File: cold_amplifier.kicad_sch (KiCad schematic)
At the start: 46 parts, among them Q1 BFP640, U1 THS4531AID

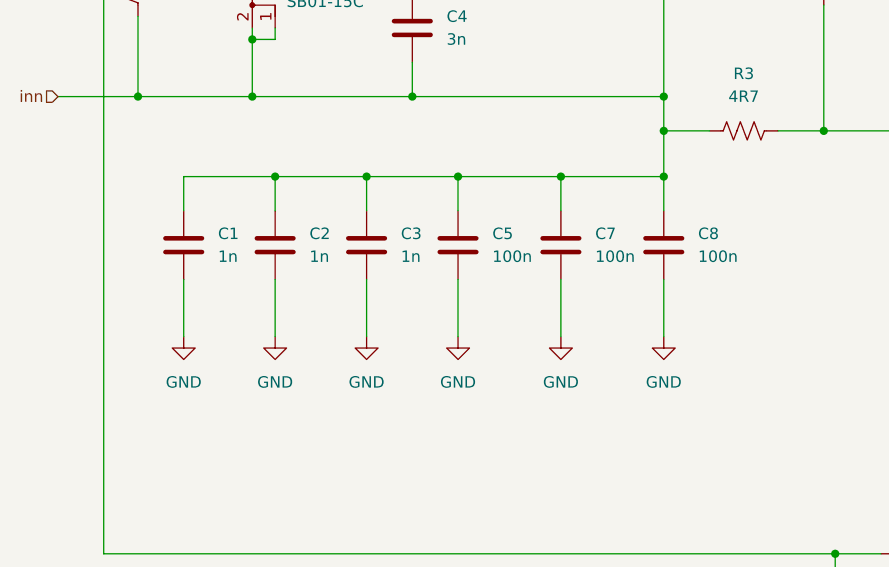
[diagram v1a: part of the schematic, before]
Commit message: Removed one pair of 1nF and 100nF capacitors connected to pin 2 of the BFP640 to allow the 100nF to be closer to the pin
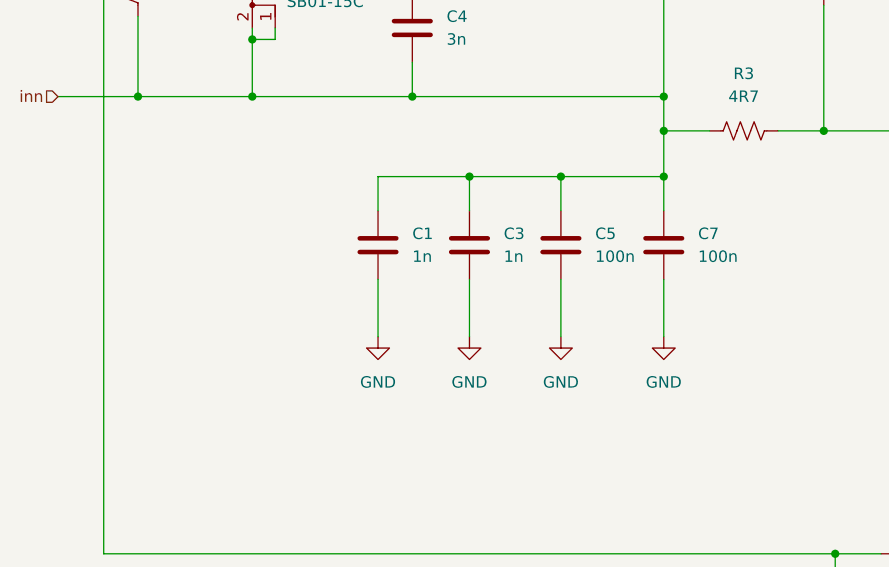
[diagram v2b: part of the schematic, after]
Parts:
- removed C2: 1n, Capacitor_SMD:C_0603_1608Metric, symbol Device:C
- removed C8: 100n, Capacitor_SMD:C_1206_3216Metric, symbol Device:C
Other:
- moved on the sheet: C1, C3, C5, C7

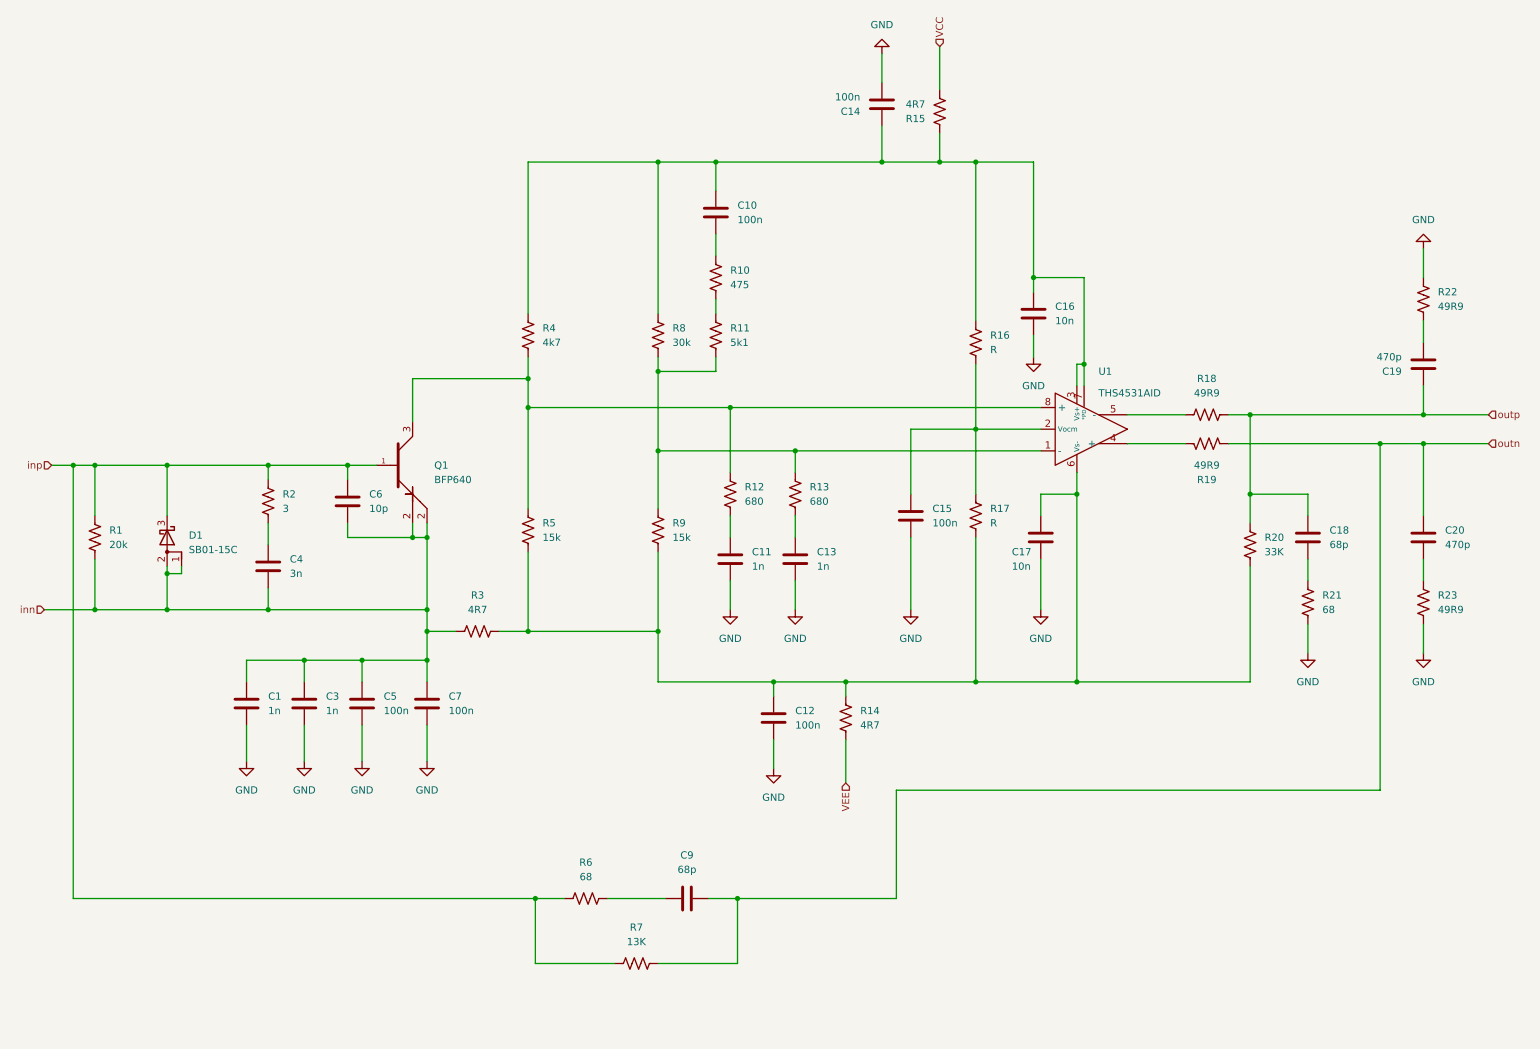
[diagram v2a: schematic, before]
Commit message: Moved connectors SiPM flex connectorsto both sides; rectangular vias stitching pattern
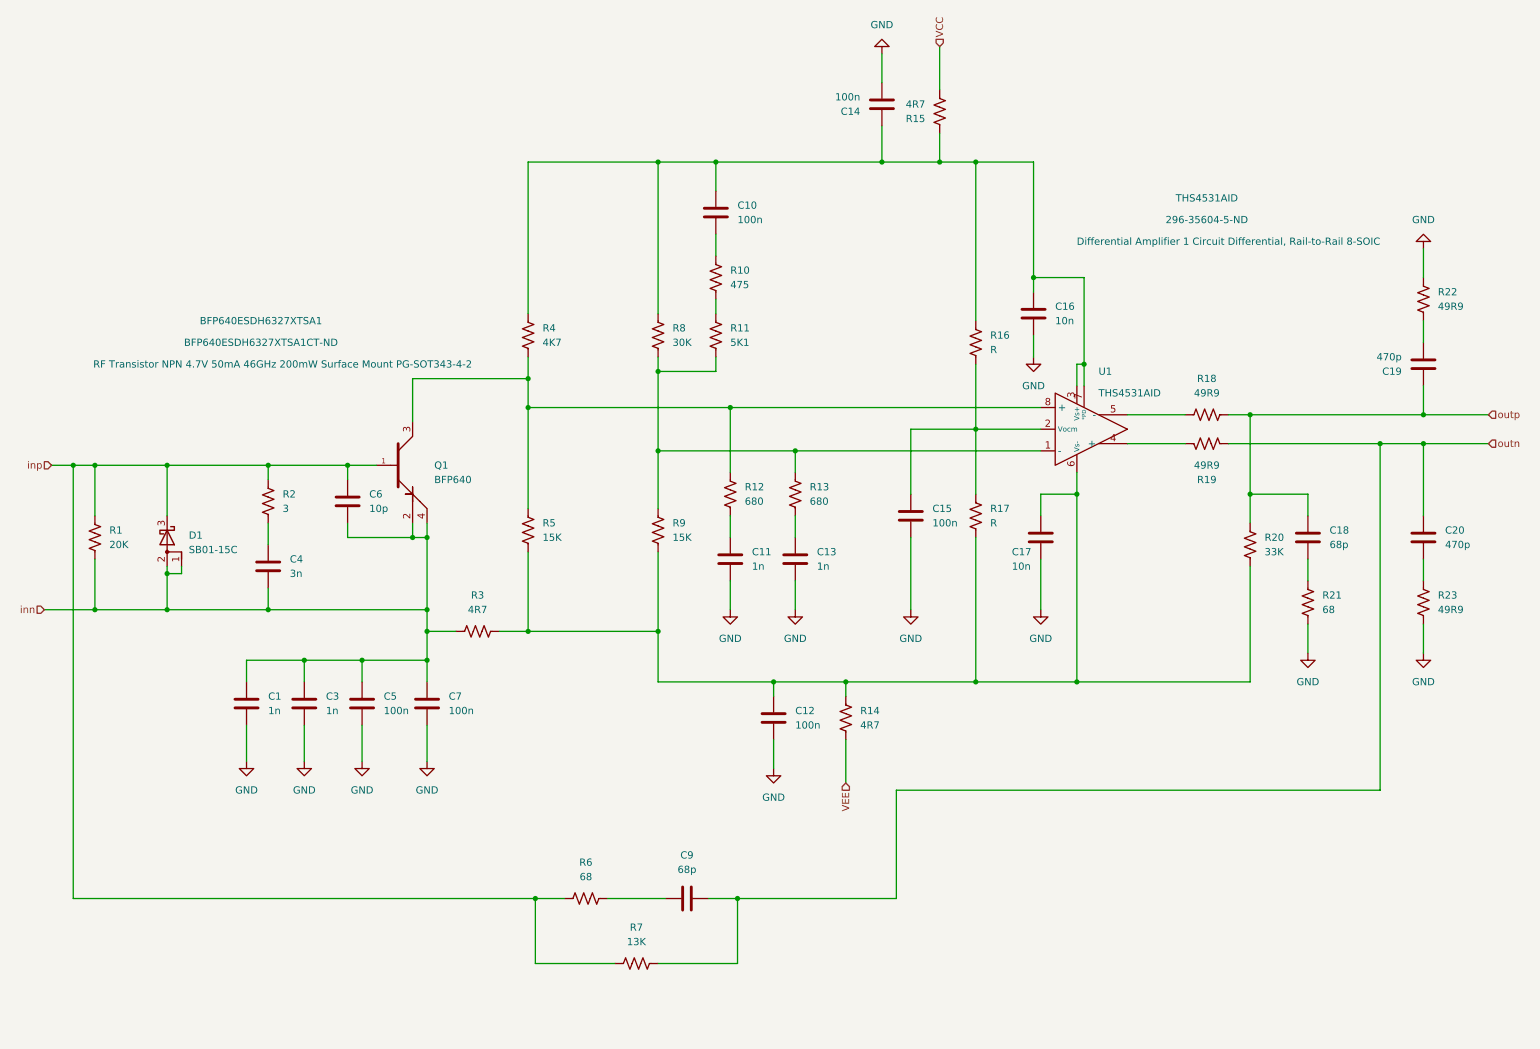
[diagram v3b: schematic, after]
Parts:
- C10, C12, C14, C15, C5, C7: Digikey Part Number (none) -> 490-GRM3195C2A104JA01DCT-ND; Manufacturer (none) -> Murata Electronics; Part Number (none) -> GRM3195C2A104JA01D
- D1: Digikey Part Number (none) -> SB01-15C-TB-EOSCT-ND; Part Number  (none) -> SB01-15C-TB-E
- Q1: Description  (none) -> RF Transistor NPN 4.7V 50mA 46GHz 200mW Surface Mount PG-SO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; Digikey Part Number (none) -> BFP640ESDH6327XTSA1CT-ND; Part Number (none) -> BFP640ESDH6327XTSA1
- R1: value 20k -> 20K; Digikey Part Number (none) -> P20KDACT-ND; Manufacturer (none) -> Panasonic Electronic Components; Part Number (none) -> ERA-6AEB203V
- R10: Digikey Part Number (none) -> P475DACT-ND; Manufacturer (none) -> Panasonic Electronic Components; Part Number (none) -> ERA-6AEB4750V
- R11: value 5k1 -> 5K1; Digikey Part Number (none) -> P5.1KDACT-ND; Manufacturer (none) -> Panasonic Electronic Components; Part Number (none) -> ERA-6AEB512V
- R12, R13: Digikey Part Number (none) -> P680DACT-ND; Manufacturer (none) -> Panasonic Electronic Components; Part Number (none) -> ERA-6AEB681V
- R14, R15, R3: Digikey Part Number (none) -> RNCP0805FTD4R70CT-ND; Manufacturer (none) -> Stackpole Electronics Inc; Part Number (none) -> RNCP0805FTD4R70
- R18, R19, R22, R23: Digikey Part Number (none) -> P49.9DACT-ND; Manufacturer (none) -> Panasonic Electronic Components; Part Number (none) -> ERA-6AEB49R9V
- R2: Digikey Part Number (none) -> YAG5007CT-ND; Manufacturer (none) -> YAGEO; Part Number (none) -> RT0805DRD073RL
- R20: Digikey Part Number (none) -> P33KDACT-ND; Manufacturer (none) -> Panasonic Electronic Components; Part Number (none) -> ERA-6AEB333V
- R21, R6: Digikey Part Number (none) -> P68DACT-ND; Manufacturer (none) -> Panasonic Electronic Components; Part Number (none) -> ERA-6AEB680V
- R4: value 4k7 -> 4K7; Digikey Part Number (none) -> P4.7KDACT-ND; Manufacturer (none) -> Panasonic Electronic Components; Part Number (none) -> ERA-6AEB472V
- R5: value 15k -> 15K; Digikey Part Number (none) -> YAG1787CT-ND; Manufacturer (none) -> YAGEO; Part Number  (none) -> RT0805BRD0715KL
- R7: Digikey Part Number (none) -> P13KDACT-ND; Manufacturer (none) -> Panasonic Electronic Components; Part Number (none) -> ERA-6AEB133V
- R8: value 30k -> 30K; Digikey Part Number (none) -> P30KDACT-ND; Manufacturer (none) -> Panasonic Electronic Components; Part Number (none) -> ERA-6AEB303V
- R9: value 15k -> 15K; Digikey Part Number (none) -> YAG1787CT-ND; Manufacturer (none) -> YAGEO; Part Number (none) -> RT0805BRD0715KL
- U1: Digikey Part Number (none) -> 296-35604-5-ND; Part Number (none) -> THS4531AID
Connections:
- net inn: now also Q1.4

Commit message: completed BOM list; replaced 47u with 33u capacitor
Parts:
- C1, C11, C13, C3: Digikey Part Number (none) -> 490-1451-1-ND; Manufacturer (none) -> Murata Electronics; Part Number (none) -> GRM1885C1H102JA01D
- C10, C12, C14, C15, C5, C7: Digikey Part Number 490-GRM3195C2A104JA01DCT-ND -> 490-6505-1-ND; Part Number GRM3195C2A104JA01D -> GRM31C5C1H104JA01L
- C16, C17: Digikey Part Number (none) -> 490-9666-1-ND; Manufacturer (none) -> Murata Electronics; Part Number (none) -> GRM1885C1H103JA01D
- C18, C9: Digikey Part Number (none) -> 1276-1135-1-ND; Manufacturer (none) -> Samsung Electro-Mechanics; Part Number (none) -> CL10C680JB8NNNC
- C19, C20: Digikey Part Number (none) -> 1276-1168-1-ND; Manufacturer (none) -> Samsung Electro-Mechanics; Part Number (none) -> CL10C471JB8NNNC
- C4: Digikey Part Number (none) -> 490-GCM1885C1H302FA16JCT-ND; Manufacturer (none) -> Murata Electronics; Part Number (none) -> GCM1885C1H302FA16J
- C6: Digikey Part Number (none) -> 490-4766-1-ND; Manufacturer (none) -> Murata Electronics; Part Number (none) -> GCM1885C1H100JA16D
- D1: value SB01-15C -> BAR46FILM; Digikey Part Number SB01-15C-TB-EOSCT-ND -> 497-12128-1-ND; Manufacturer (none) -> STMicroelectronics; Part Number (none) -> BAR46FILM; Part Number  SB01-15C-TB-E -> (none)
- Q1: Description  RF Transistor NPN 4.7V 50mA 46GHz 200mW Surface Mount PG-SO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 -> (none); Manufacturer (none) -> Infineon Technologies
- R5: Part Number (none) -> RT0805BRD0715KL; Part Number  RT0805BRD0715KL -> (none)
- U1: Manufacturer (none) -> Texas Instruments

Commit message: Changed footprint to removed unused silkscreen symbols; silkscreen more legible; changed texts next to arrows; changed wrong 0.22u cap to 47u
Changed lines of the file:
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@@
   (junction (at 62.23 119.38) (diameter 0) (color 0 0 0 0)
   )
+  (junction (at 90.17 104.14) (diameter 0) (color 0 0 0 0)
+  )
   (junction (at 257.81 90.17) (diameter 0) (color 0 0 0 0)
   )
@@
   (junction (at 204.47 99.06) (diameter 0) (color 0 0 0 0)
   )
-  (junction (at 87.63 106.68) (diameter 0) (color 0 0 0 0)
-  )
   (junction (at 170.18 40.64) (diameter 0) (color 0 0 0 0)
   )
@@
   (junction (at 234.95 85.09) (diameter 0) (color 0 0 0 0)
   )
+  (junction (at 87.63 104.14) (diameter 0) (color 0 0 0 0)
+  )
   (junction (at 186.69 87.63) (diameter 0) (color 0 0 0 0)
   )
@@
   (junction (at 27.94 93.98) (diameter 0) (color 0 0 0 0)
   )
-  (junction (at 90.17 106.68) (diameter 0) (color 0 0 0 0)
-  )
   (junction (at 44.45 119.38) (diameter 0) (color 0 0 0 0)
   )
@@
     (stroke (width 0) (type default))
   )
-  (wire (pts (xy 90.17 104.14) (xy 90.17 106.68))
+  (wire (pts (xy 90.17 104.14) (xy 90.17 119.38))
     (stroke (width 0) (type default))
   )
@@
     (stroke (width 0) (type default))
   )
-  (wire (pts (xy 90.17 106.68) (xy 87.63 106.68))
-    (stroke (width 0) (type default))
-  )
   (wire (pts (xy 68.58 139.7) (xy 68.58 146.05))
     (stroke (width 0) (type default))
@@
     (stroke (width 0) (type default))
   )
-  (wire (pts (xy 90.17 119.38) (xy 90.17 106.68))
-    (stroke (width 0) (type default))
-  )
   (wire (pts (xy 196.85 40.64) (xy 196.85 60.96))
     (stroke (width 0) (type default))
@@
     (stroke (width 0) (type default))
   )
+  (wire (pts (xy 87.63 104.14) (xy 90.17 104.14))
+    (stroke (width 0) (type default))
+  )

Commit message: Solved error in netlist; input connector was in a mirror configuration; solved also DB15 error in netlist
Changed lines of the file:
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@@
       (effects (font (size 1.27 1.27)) hide)
     )
-    (property "Part Number" "BFP640ESDH6327XTSA1" (at 85.09 68.58 0)
-      (effects (font (size 1.27 1.27)))
-    )
-    (property "Digikey Part Number" "BFP640ESDH6327XTSA1CT-ND" (at 83.82 71.12 0)
-      (effects (font (size 1.27 1.27)))
-    )
-    (property "Description" "RF Transistor NPN 4.7V 50mA 46GHz 200mW Surface Mount PG-SOT343-4-2" (at 86.36 73.66 0)
+    (property "Part Number" "BFP640ESDH6327XTSA1" (at 66.04 68.58 0)
+      (effects (font (size 1.27 1.27)))
+    )
+    (property "Digikey Part Number" "BFP640ESDH6327XTSA1CT-ND" (at 64.77 71.12 0)
+      (effects (font (size 1.27 1.27)))
+    )
+    (property "Description" "RF Transistor NPN 4.7V 50mA 46GHz 200mW Surface Mount PG-SOT343-4-2" (at 67.31 73.66 0)
       (effects (font (size 1.27 1.27)))
     )
@@
       (effects (font (size 1.27 1.27)) hide)
     )
-    (property "Manufacturer" "Texas Instruments" (at 205.74 87.63 0)
-      (effects (font (size 1.27 1.27)))
-    )
+    (property "Manufacturer" "Texas Instruments" (at 227.33 44.45 0)
+      (effects (font (size 1.27 1.27)))
+    )

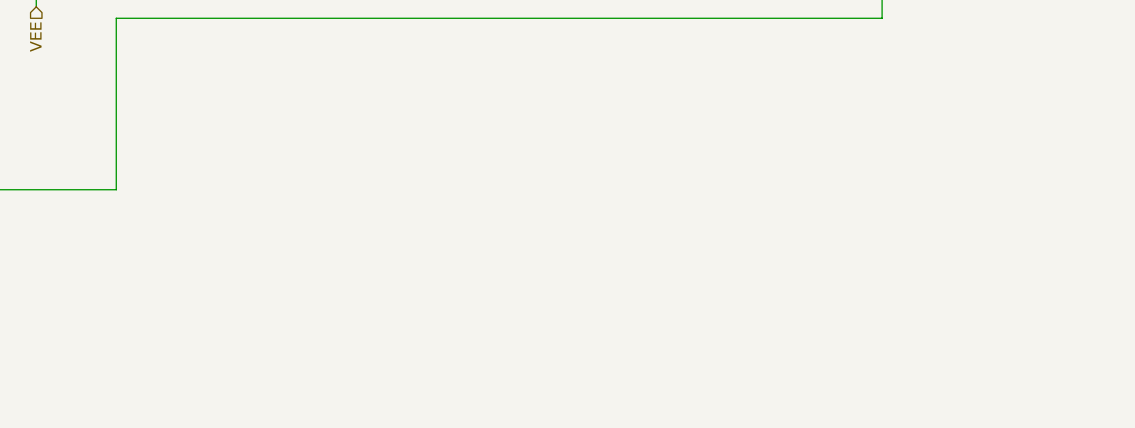
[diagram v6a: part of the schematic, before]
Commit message: Version tested at coldbox March 2026
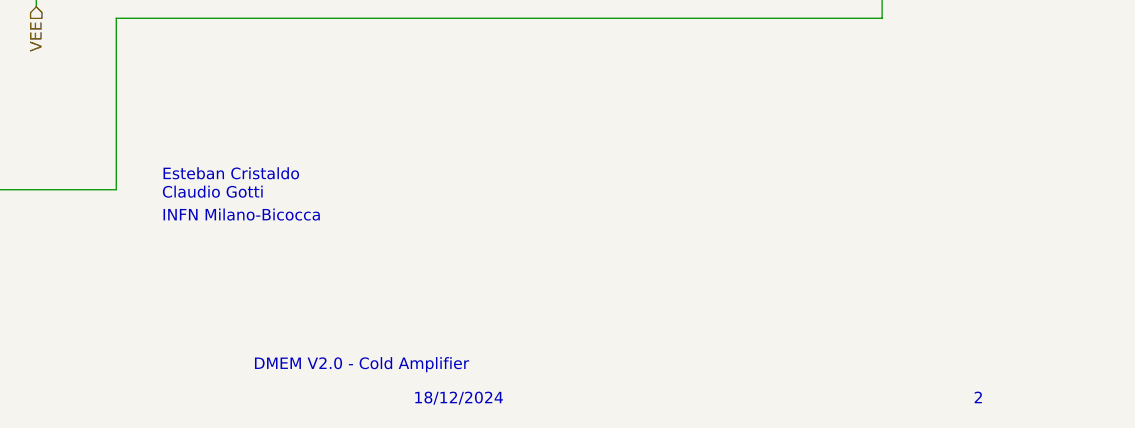
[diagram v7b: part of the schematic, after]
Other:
- note added: "18/12/2024"
- note added: "2"
- note added: "DMEM V2.0 - Cold Amplifier"
- note added: "Esteban Cristaldo Claudio Gotti"
- note added: "INFN Milano-Bicocca"
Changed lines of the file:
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@@
     (stroke (width 0) (type default))
+  )
+  (text "18/12/2024\n" (at 205.74 194.31 0)
+    (effects (font (size 1.27 1.27)) (justify left bottom))
+  )
+  (text "DMEM V2.0 - Cold Amplifier" (at 187.96 190.5 0)
+    (effects (font (size 1.27 1.27)) (justify left bottom))
+  )
+  (text "INFN Milano-Bicocca\n" (at 177.8 173.99 0)
+    (effects (font (size 1.27 1.27)) (justify left bottom))
+  )
+  (text "2\n" (at 267.97 194.31 0)
+    (effects (font (size 1.27 1.27)) (justify left bottom))
+  )
+  (text "Esteban Cristaldo \nClaudio Gotti\n" (at 177.8 171.45 0)
+    (effects (font (size 1.27 1.27)) (justify left bottom))
   )
   (hierarchical_label "inn" (shape input) (at 22.86 119.38 180) (fields_autoplaced)
